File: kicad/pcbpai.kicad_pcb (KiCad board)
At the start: 2 copper layers, 68 x 98 mm, 24 parts, among them J1 Fuse, J10 Conn_01x02_Socket, J11 Conn_01x02_Socket, J12 Conn_01x02_Socket, J2 Conn_01x08_Socket, J3 Input 24 V, J4 Boton Encendido, J5 Parada de Emergencia, J6 Conn_01x08_Socket, J7 Raspberry GPIO, J8 Conn_01x02_Socket, J9 Conn_01x02_Socket, M1 MountingHole_2.5mm_Pad, M2 MountingHole_2.5mm_Pad, M3 MountingHole_2.5mm_Pad, M4 MountingHole_2.5mm_Pad, U6 ATtiny85-20P

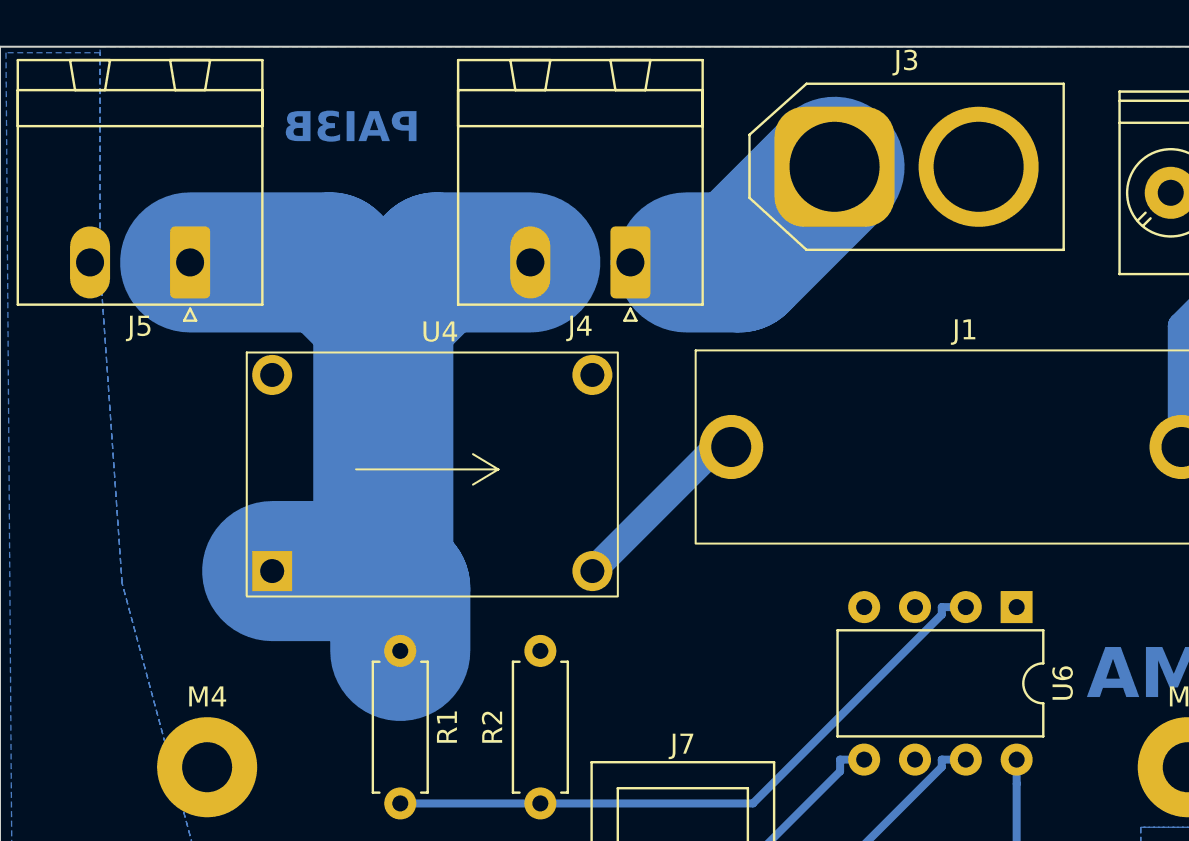
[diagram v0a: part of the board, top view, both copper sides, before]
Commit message: unfix xt60 polarity
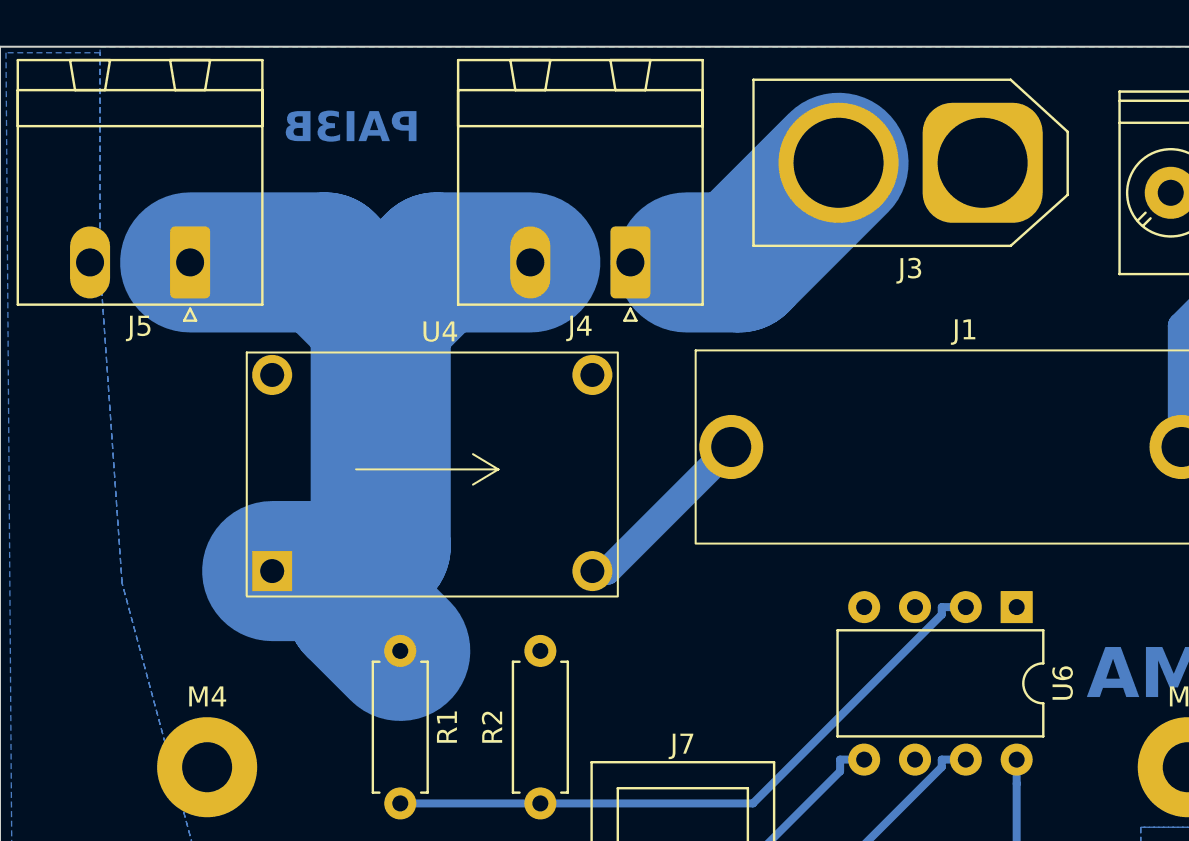
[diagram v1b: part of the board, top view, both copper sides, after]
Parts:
- moved J3 7.40 mm to (159.1, 49.8), turned to 180 degrees
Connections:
- J3 pad 1: +24V -> GND
- J3 pad 2: GND -> +24V

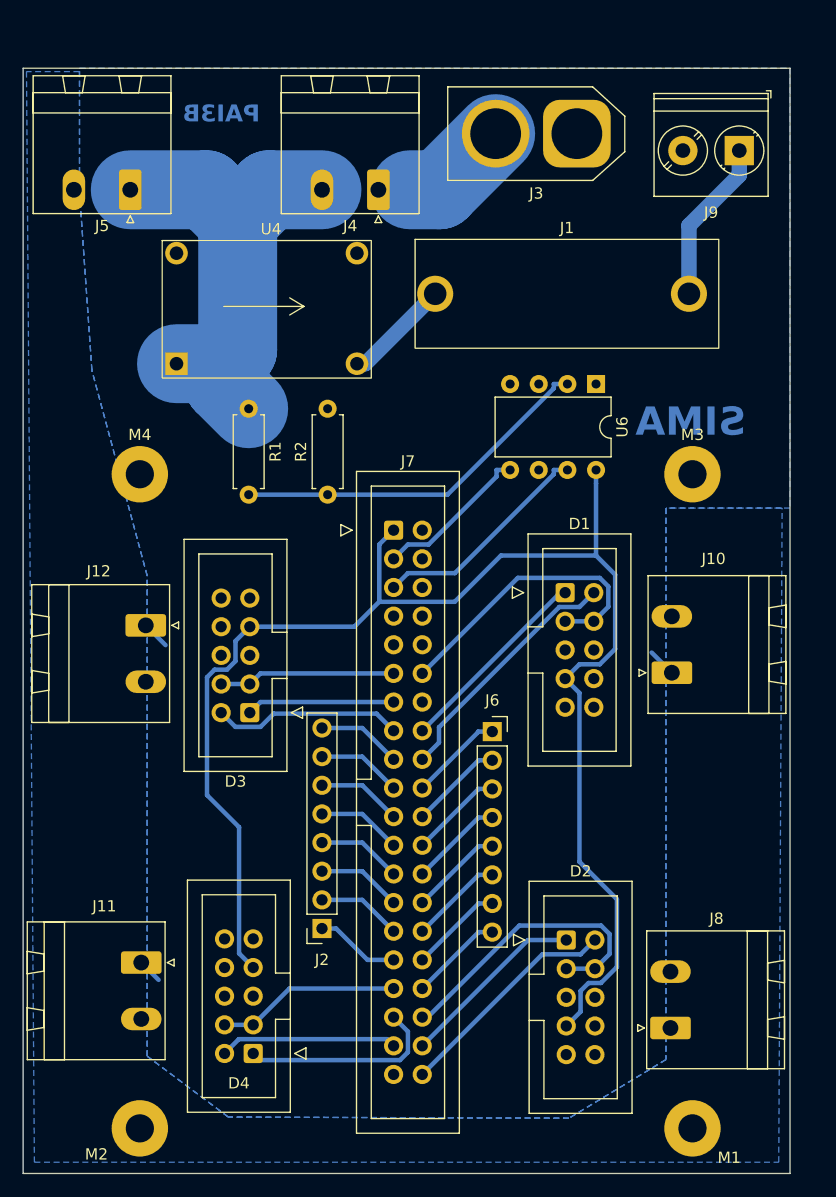
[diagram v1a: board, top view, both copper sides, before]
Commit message: change switch and fuse symbols
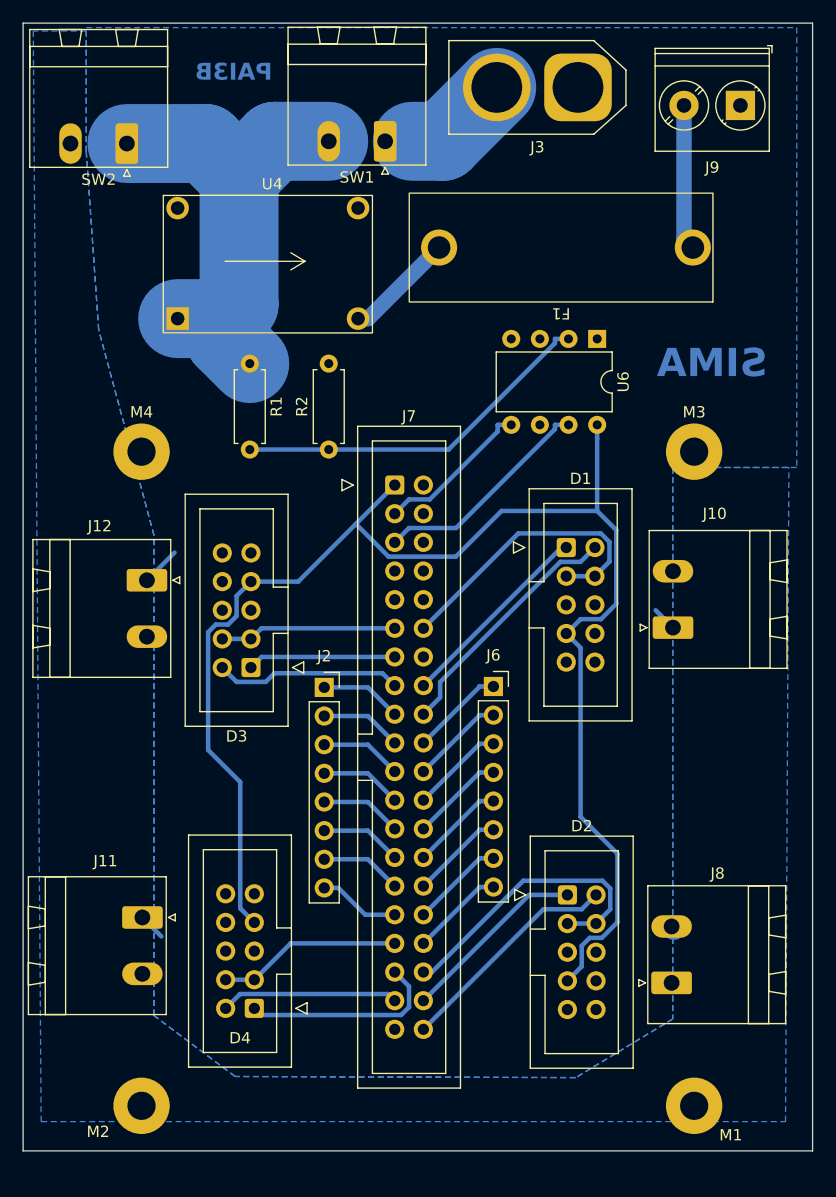
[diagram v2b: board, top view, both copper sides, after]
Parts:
- removed J1: Fuse, PAI:fuse
- removed J4: Boton Encendido, Connector_Phoenix_MSTB:PhoenixContact_MSTBA_2,5_2-G_1x02_P5.00mm_Horizontal
- removed J5: Parada de Emergencia, Connector_Phoenix_MSTB:PhoenixContact_MSTBA_2,5_2-G_1x02_P5.00mm_Horizontal
- added F1: Fuse, PAI:fuse, F.Cu at (169.4, 59.9)
- added SW1: SW_SPST, Connector_Phoenix_MSTB:PhoenixContact_MSTBA_2,5_2-G_1x02_P5.00mm_Horizontal, F.Cu at (142.1, 50.5)
- added SW2: SW_Push_Open, Connector_Phoenix_MSTB:PhoenixContact_MSTBA_2,5_2-G_1x02_P5.00mm_Horizontal, F.Cu at (119.2, 50.7)
- moved J2 21.4 mm to (136.7, 98.9), turned to 0 degrees
- moved J3 4.10 mm to (159.2, 45.7)
- moved D4 4.00 mm to (130.5, 127.4)
- moved J12 4.00 mm to (121.0, 89.4)
- moved U4 4.00 mm to (123.7, 66.2)
- moved D1 4.00 mm to (158.2, 86.5)
- moved D2 4.00 mm to (158.3, 117.3)
- moved D3 4.00 mm to (130.2, 97.1)
- moved J10 4.00 mm to (167.6, 93.6)
- moved J11 4.00 mm to (120.6, 119.3)
- moved J6 4.00 mm to (151.7, 98.8)
- moved J7 4.00 mm to (142.9, 81.0)
- moved J8 4.00 mm to (167.5, 125.1)
- moved J9 4.00 mm to (173.6, 47.3)
- moved R1 4.00 mm to (130.1, 70.2)
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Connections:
- J7 pad 17: Net-(J2-Pin_8) -> Net-(J2-Pin_1)
- J7 pad 19: Net-(J2-Pin_7) -> Net-(J2-Pin_2)
- J7 pad 21: Net-(J2-Pin_6) -> Net-(J2-Pin_3)
- J7 pad 23: Net-(J2-Pin_5) -> Net-(J2-Pin_4)
- J7 pad 25: Net-(J2-Pin_4) -> Net-(J2-Pin_5)
- J7 pad 27: Net-(J2-Pin_3) -> Net-(J2-Pin_6)
- J7 pad 29: Net-(J2-Pin_2) -> Net-(J2-Pin_7)
- J7 pad 31: Net-(J2-Pin_1) -> Net-(J2-Pin_8)
- J9 pad 1: Net-(J1-Pin_2) -> GND
- J9 pad 2: GND -> Net-(J9-Pin_2)
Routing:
- net Net-(J1-Pin_2): track 14.5 -> 0.00 mm
- net Net-(J9-Pin_2): track 0.00 -> 12.9 mm
- net Net-(SW1-B): track 41.6 -> 42.6 mm
- net +24V: track 12.5 -> 11.9 mm
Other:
- board size 68 x 98 mm -> 70 x 100 mm
